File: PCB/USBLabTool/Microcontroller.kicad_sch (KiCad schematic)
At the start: 17 parts, among them J1 Conn_01x06_Pin, J2 Conn_02x12_Odd_Even, SW1 SW_Push, U12 STM32H562VGTx, Y1 32.768kHz

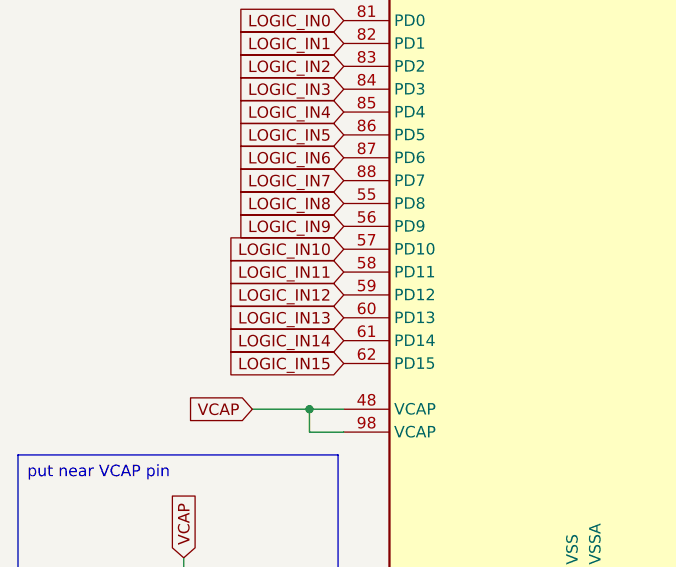
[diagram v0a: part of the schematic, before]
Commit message: Updated schematic and PCB
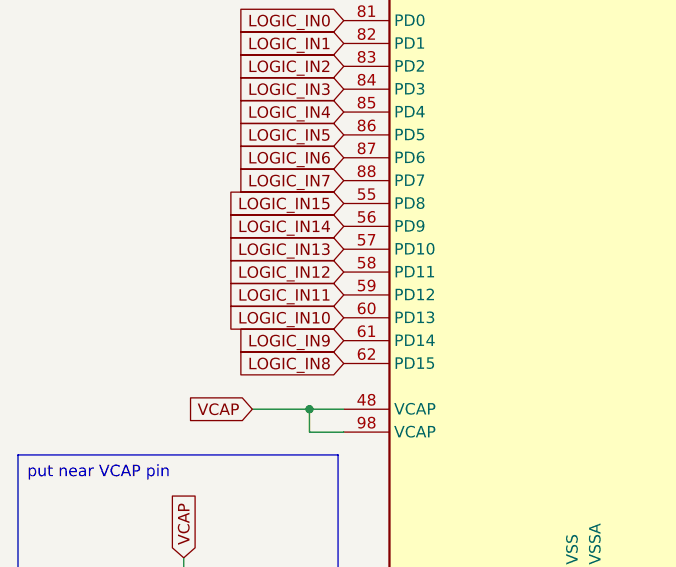
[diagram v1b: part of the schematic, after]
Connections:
- net LOGIC_IN10: now also U12.60 (PD13); no longer U12.57 (PD10)
- net LOGIC_IN11: now also U12.59 (PD12); no longer U12.58 (PD11)
- net LOGIC_IN12: now also U12.58 (PD11); no longer U12.59 (PD12)
- net LOGIC_IN13: now also U12.57 (PD10); no longer U12.60 (PD13)
- net LOGIC_IN14: now also U12.56 (PD9); no longer U12.61 (PD14)
- net LOGIC_IN15: now also U12.55 (PD8); no longer U12.62 (PD15)
- net LOGIC_IN8: now also U12.62 (PD15); no longer U12.55 (PD8)
- net LOGIC_IN9: now also U12.61 (PD14); no longer U12.56 (PD9)

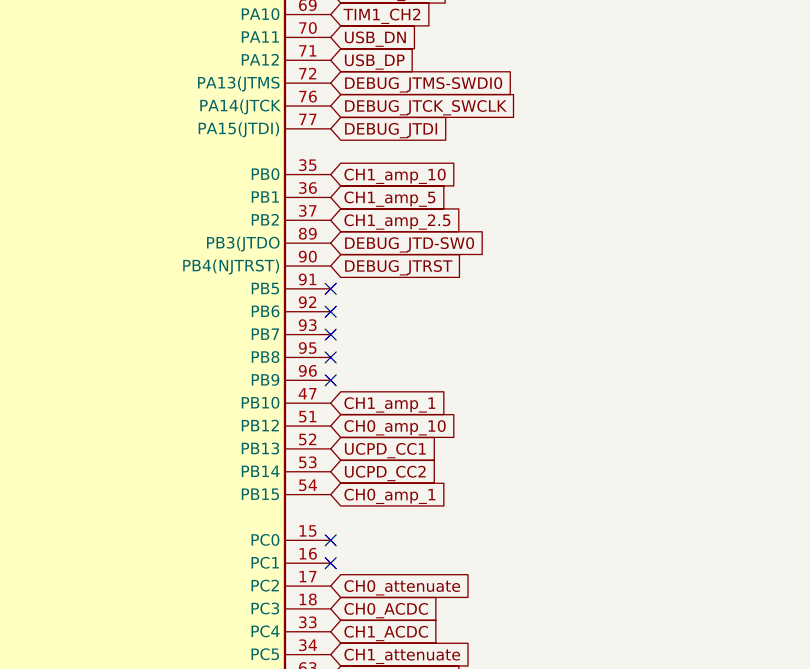
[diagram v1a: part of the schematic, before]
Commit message: swap MCU  pins for routing
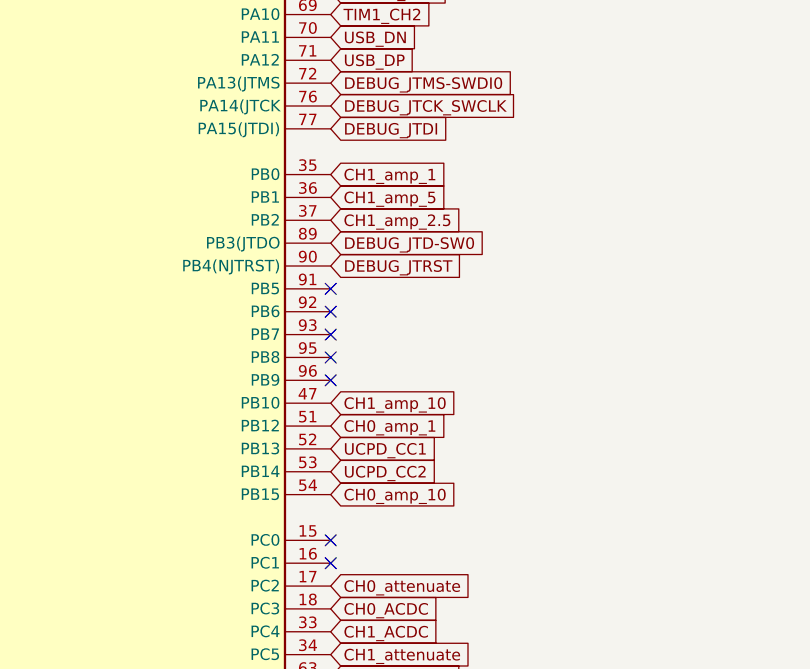
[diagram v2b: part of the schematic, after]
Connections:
- net CH0_amp_1: now also U12.51 (PB12); no longer U12.54 (PB15)
- net CH0_amp_10: now also U12.54 (PB15); no longer U12.51 (PB12)
- net CH1_amp_1: now also U12.35 (PB0); no longer U12.47 (PB10)
- net CH1_amp_10: now also U12.47 (PB10); no longer U12.35 (PB0)

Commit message: continue PCB layout
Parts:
- J2: footprint Connector_JST:JST_PHD_S24B-PHDSS_2x12_P2.00mm_Horizontal -> userfp:OST_302-R241
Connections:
- net +3.3V: now also J2.2 (Pin_2); no longer J2.24 (Pin_24)
- net +5V: now also J2.1 (Pin_1); no longer J2.23 (Pin_23)
- net CH0_ACDC: now also J2.7 (Pin_7); no longer J2.17 (Pin_17)
- net CH1_ACDC: now also J2.8 (Pin_8); no longer J2.18 (Pin_18)
- net DAC1_OUT1: now also J2.3 (Pin_3); no longer J2.21 (Pin_21)
- net DAC1_OUT2: now also J2.4 (Pin_4); no longer J2.22 (Pin_22)
- net GND: now also J2.5 (Pin_5); no longer J2.19 (Pin_19)
- net GNDA: now also J2.6 (Pin_6); no longer J2.20 (Pin_20)
- net LOGIC_INP0: now also J2.23 (Pin_23); no longer J2.1 (Pin_1)
- net LOGIC_INP1: now also J2.21 (Pin_21); no longer J2.3 (Pin_3)
- net LOGIC_INP10: now also J2.20 (Pin_20); no longer J2.6 (Pin_6)
- net LOGIC_INP11: now also J2.18 (Pin_18); no longer J2.8 (Pin_8)
- net LOGIC_INP12: now also J2.16 (Pin_16); no longer J2.10 (Pin_10)
- net LOGIC_INP13: now also J2.14 (Pin_14); no longer J2.12 (Pin_12)
- net LOGIC_INP14: now also J2.12 (Pin_12); no longer J2.14 (Pin_14)
- net LOGIC_INP15: now also J2.10 (Pin_10); no longer J2.16 (Pin_16)
- net LOGIC_INP2: now also J2.19 (Pin_19); no longer J2.5 (Pin_5)
- net LOGIC_INP3: now also J2.17 (Pin_17); no longer J2.7 (Pin_7)
- net LOGIC_INP4: now also J2.15 (Pin_15); no longer J2.9 (Pin_9)
- net LOGIC_INP5: now also J2.13 (Pin_13); no longer J2.11 (Pin_11)
- net LOGIC_INP6: now also J2.11 (Pin_11); no longer J2.13 (Pin_13)
- net LOGIC_INP7: now also J2.9 (Pin_9); no longer J2.15 (Pin_15)
- net LOGIC_INP8: now also J2.24 (Pin_24); no longer J2.2 (Pin_2)
- net LOGIC_INP9: now also J2.22 (Pin_22); no longer J2.4 (Pin_4)
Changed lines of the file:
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@@
 (kicad_sch
-	(version 20231120)
+	(version 20250114)
 	(generator "eeschema")
-	(generator_version "8.0")
+	(generator_version "9.0")
 	(paper "A3")

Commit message: some very small wirings, and layout
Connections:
- net +5V is gone; now on net CH0_ACDC: J2.1 (Pin_1)
- net +3.3V: no longer J2.2 (Pin_2)
- net CH0_ACDC: no longer J2.7 (Pin_7)
- net CH1_ACDC: now also J2.2 (Pin_2); no longer J2.8 (Pin_8)
- net DAC1_OUT1: now also J2.5 (Pin_5); no longer J2.3 (Pin_3)
- net DAC1_OUT2: now also J2.6 (Pin_6); no longer J2.4 (Pin_4)
- net GND: now also J2.3 (Pin_3), J2.7 (Pin_7); no longer J2.5 (Pin_5)
- net GNDA: now also J2.4 (Pin_4), J2.8 (Pin_8); no longer J2.6 (Pin_6)

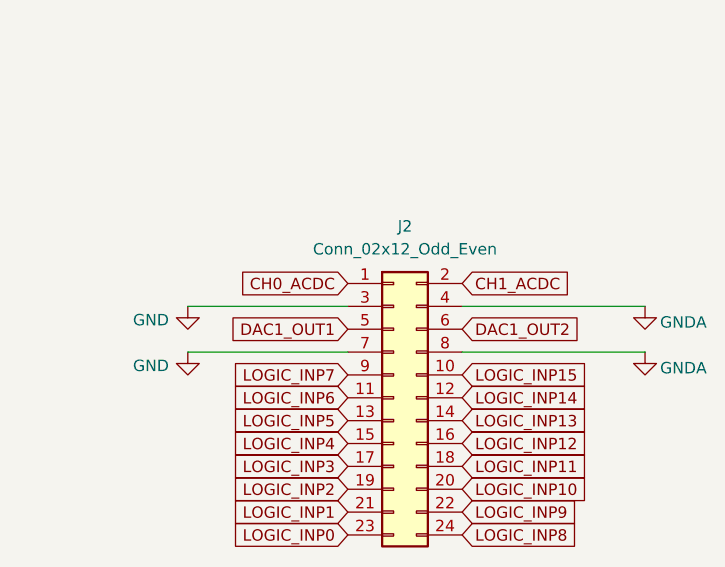
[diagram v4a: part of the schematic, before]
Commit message: fix the pin out
never be lazy and stupid at the same time 👎
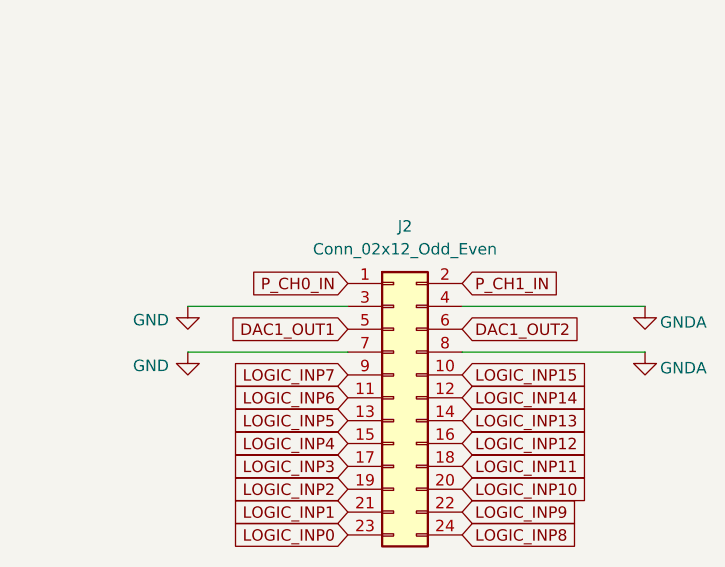
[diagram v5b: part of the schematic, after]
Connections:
- net CH0_ACDC: no longer J2.1 (Pin_1)
- net CH1_ACDC: no longer J2.2 (Pin_2)
- new net P_CH0_IN: J2.1 (Pin_1)
- new net P_CH1_IN: J2.2 (Pin_2)

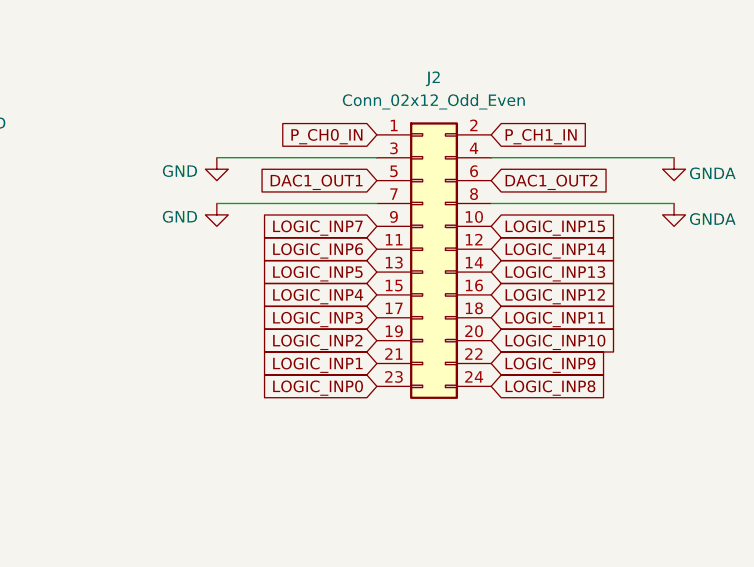
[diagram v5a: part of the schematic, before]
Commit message: rearrange pins
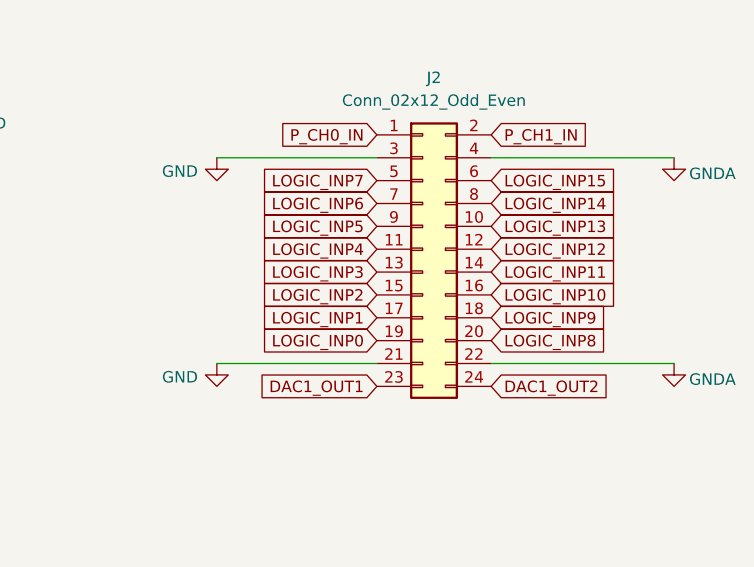
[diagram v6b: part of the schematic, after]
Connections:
- net DAC1_OUT1: now also J2.23 (Pin_23); no longer J2.5 (Pin_5)
- net DAC1_OUT2: now also J2.24 (Pin_24); no longer J2.6 (Pin_6)
- net GND: now also J2.21 (Pin_21); no longer J2.7 (Pin_7)
- net GNDA: now also J2.22 (Pin_22); no longer J2.8 (Pin_8)
- net LOGIC_INP0: now also J2.19 (Pin_19); no longer J2.23 (Pin_23)
- net LOGIC_INP1: now also J2.17 (Pin_17); no longer J2.21 (Pin_21)
- net LOGIC_INP10: now also J2.16 (Pin_16); no longer J2.20 (Pin_20)
- net LOGIC_INP11: now also J2.14 (Pin_14); no longer J2.18 (Pin_18)
- net LOGIC_INP12: now also J2.12 (Pin_12); no longer J2.16 (Pin_16)
- net LOGIC_INP13: now also J2.10 (Pin_10); no longer J2.14 (Pin_14)
- net LOGIC_INP14: now also J2.8 (Pin_8); no longer J2.12 (Pin_12)
- net LOGIC_INP15: now also J2.6 (Pin_6); no longer J2.10 (Pin_10)
- net LOGIC_INP2: now also J2.15 (Pin_15); no longer J2.19 (Pin_19)
- net LOGIC_INP3: now also J2.13 (Pin_13); no longer J2.17 (Pin_17)
- net LOGIC_INP4: now also J2.11 (Pin_11); no longer J2.15 (Pin_15)
- net LOGIC_INP5: now also J2.9 (Pin_9); no longer J2.13 (Pin_13)
- net LOGIC_INP6: now also J2.7 (Pin_7); no longer J2.11 (Pin_11)
- net LOGIC_INP7: now also J2.5 (Pin_5); no longer J2.9 (Pin_9)
- net LOGIC_INP8: now also J2.20 (Pin_20); no longer J2.24 (Pin_24)
- net LOGIC_INP9: now also J2.18 (Pin_18); no longer J2.22 (Pin_22)

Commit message: Added holes to PCB schematic, fixed DRC
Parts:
- added H1, H2, H3, H4: MountingHole, MountingHole:MountingHole_2.2mm_M2, symbol Mechanical:MountingHole

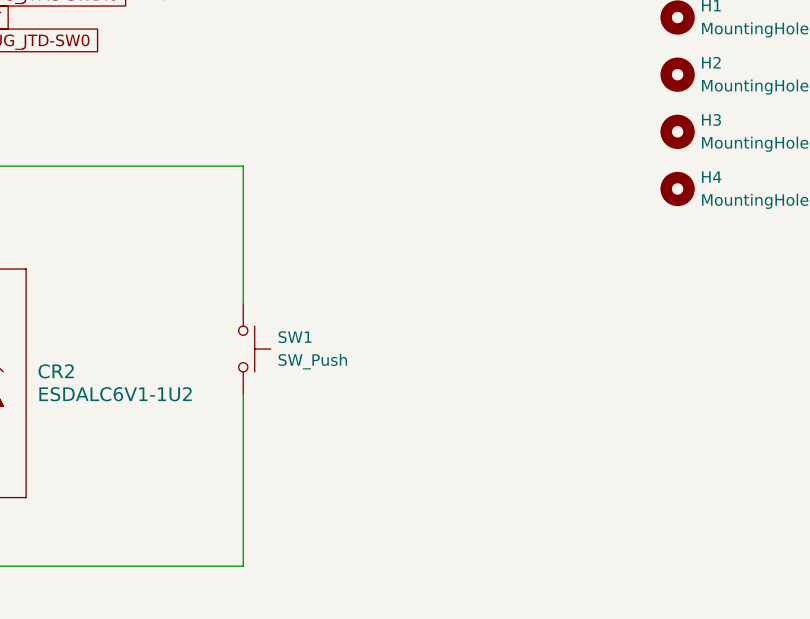
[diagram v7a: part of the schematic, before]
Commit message: fix footprint and change button
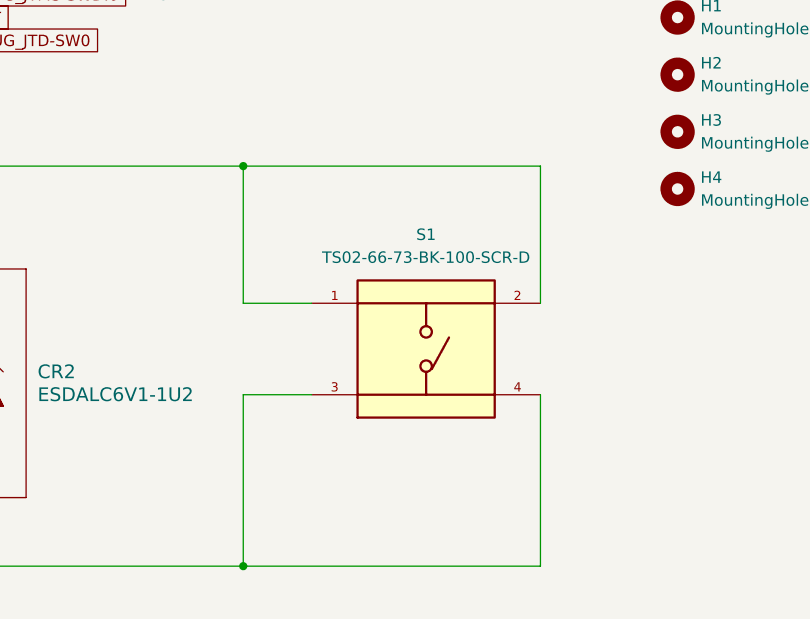
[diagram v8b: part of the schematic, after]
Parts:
- removed SW1: SW_Push, Button_Switch_THT:SW_PUSH_6mm_H7.3mm, symbol Switch:SW_Push
- added S1: TS02-66-73-BK-100-SCR-D, userfp:SW_TS02-66-73-BK-100-SCR-D, symbol TS02-66-73-BK-100-SCR-D:TS02-66-73-BK-100-SCR-D
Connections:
- net GND: now also S1.3, S1.4
- net NRST: now also S1.1, S1.2
